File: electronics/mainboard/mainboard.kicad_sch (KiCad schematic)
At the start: 53 parts, among them J1 Conn_01x09, J10 Conn_01x08, J11 Conn_01x08, J12 Conn_01x08, J13 Conn_02x18_Odd_Even, J14 Conn_01x08, J15 Conn_01x08, J16 Conn_01x10, J17 Conn_02x03_Odd_Even, J2 Conn_01x09, J3 Conn_01x09, J4 Conn_01x09, J5 Conn_01x09, J6 Conn_01x09, J7 Conn_01x09, J8 Conn_01x09, J9 Conn_01x09

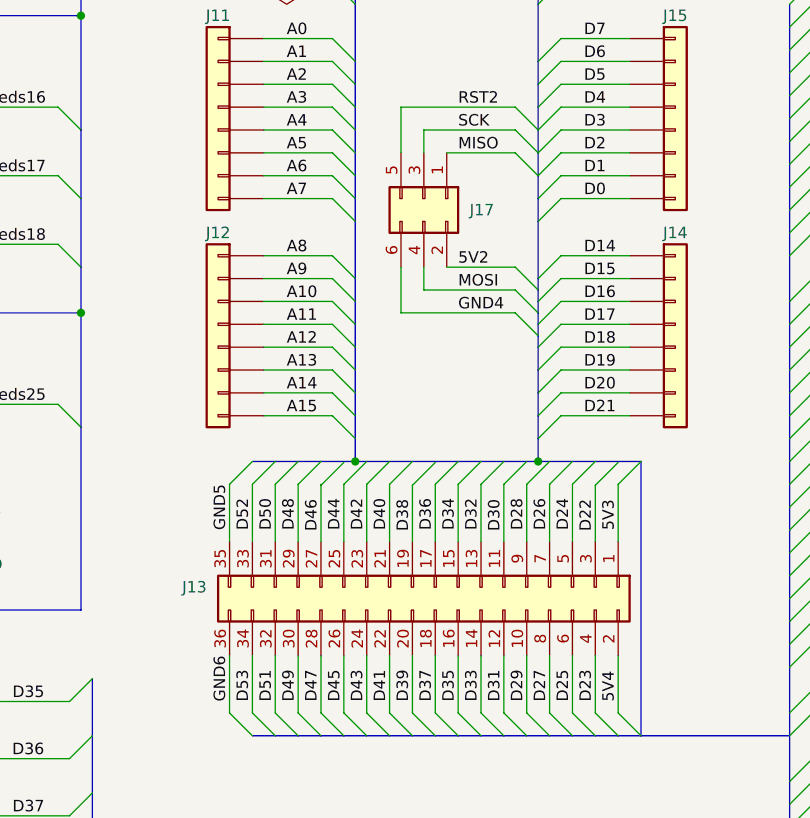
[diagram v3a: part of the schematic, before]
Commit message: place parts on pcb
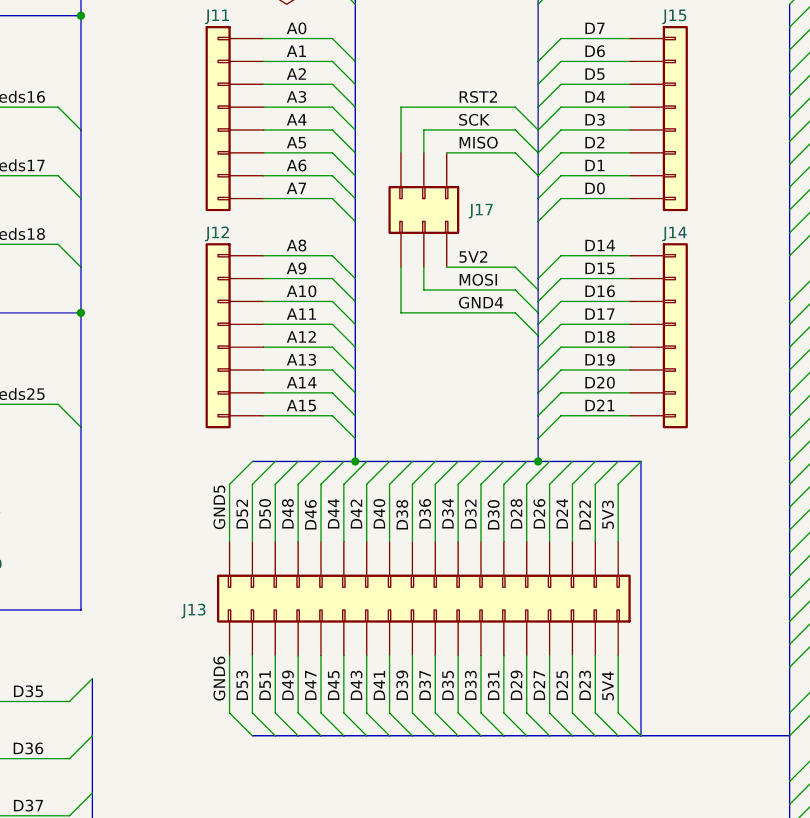
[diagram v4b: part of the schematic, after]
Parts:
- J17: footprint Connector_PinHeader_2.54mm:PinHeader_2x03_P2.54mm_Vertical_SMD -> Connector_PinSocket_2.54mm:PinSocket_2x03_P2.54mm_Vertical_SMD
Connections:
- net 5V3: now also J13.2 (Pin_2); no longer J13.1 (Pin_1)
- net 5V4: now also J13.1 (Pin_1); no longer J13.2 (Pin_2)
- net D22: now also J13.4 (Pin_4); no longer J13.3 (Pin_3)
- net D23: now also J13.3 (Pin_3); no longer J13.4 (Pin_4)
- net D24: now also J13.6 (Pin_6); no longer J13.5 (Pin_5)
- net D25: now also J13.5 (Pin_5); no longer J13.6 (Pin_6)
- net D26: now also J13.8 (Pin_8); no longer J13.7 (Pin_7)
- net D27: now also J13.7 (Pin_7); no longer J13.8 (Pin_8)
- net D28: now also J13.10 (Pin_10); no longer J13.9 (Pin_9)
- net D29: now also J13.9 (Pin_9); no longer J13.10 (Pin_10)
- net D30: now also J13.12 (Pin_12); no longer J13.11 (Pin_11)
- net D31: now also J13.11 (Pin_11); no longer J13.12 (Pin_12)
- net D32: now also J13.14 (Pin_14); no longer J13.13 (Pin_13)
- net D33: now also J13.13 (Pin_13); no longer J13.14 (Pin_14)
- net D34: now also J13.16 (Pin_16); no longer J13.15 (Pin_15)
- net D35: now also J13.15 (Pin_15); no longer J13.16 (Pin_16)
- net D36: now also J13.18 (Pin_18); no longer J13.17 (Pin_17)
- net D37: now also J13.17 (Pin_17); no longer J13.18 (Pin_18)
- net D38: now also J13.20 (Pin_20); no longer J13.19 (Pin_19)
- net D39: now also J13.19 (Pin_19); no longer J13.20 (Pin_20)
- net D40: now also J13.22 (Pin_22); no longer J13.21 (Pin_21)
- net D41: now also J13.21 (Pin_21); no longer J13.22 (Pin_22)
- net D42: now also J13.24 (Pin_24); no longer J13.23 (Pin_23)
- net D43: now also J13.23 (Pin_23); no longer J13.24 (Pin_24)
- net D44: now also J13.26 (Pin_26); no longer J13.25 (Pin_25)
- net D45: now also J13.25 (Pin_25); no longer J13.26 (Pin_26)
- net D46: now also J13.28 (Pin_28); no longer J13.27 (Pin_27)
- net D47: now also J13.27 (Pin_27); no longer J13.28 (Pin_28)
- net D48: now also J13.30 (Pin_30); no longer J13.29 (Pin_29)
- net D49: now also J13.29 (Pin_29); no longer J13.30 (Pin_30)
- net D50: now also J13.32 (Pin_32); no longer J13.31 (Pin_31)
- net D51: now also J13.31 (Pin_31); no longer J13.32 (Pin_32)
- net D52: now also J13.34 (Pin_34); no longer J13.33 (Pin_33)
- net D53: now also J13.33 (Pin_33); no longer J13.34 (Pin_34)
- net GND5: now also J13.36 (Pin_36); no longer J13.35 (Pin_35)
- net GND6: now also J13.35 (Pin_35); no longer J13.36 (Pin_36)
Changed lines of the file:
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@@
     (stroke (width 0) (type default) (color 0 0 0 0))
   )
-  (bus_entry (at 166.37 95.3582) (size 2.54 -2.54)
+  (bus_entry (at 166.37 95.25) (size 2.54 -2.54)
     (stroke (width 0) (type default) (color 0 0 0 0))
   )
@@
     (stroke (width 0) (type default) (color 0 0 0 0))
   )
-  (bus_entry (at 146.05 95.3582) (size 2.54 -2.54)
+  (bus_entry (at 146.05 95.25) (size 2.54 -2.54)
     (stroke (width 0) (type default) (color 0 0 0 0))
   )
@@
     (stroke (width 0) (type default) (color 0 0 0 0))
   )
-  (bus_entry (at 135.89 95.3582) (size 2.54 -2.54)
+  (bus_entry (at 135.89 95.25) (size 2.54 -2.54)
     (stroke (width 0) (type default) (color 0 0 0 0))
   )
@@
     (stroke (width 0) (type default) (color 0 0 0 0))
   )
-  (bus (pts (xy 151.13 92.71) (xy 146.05 92.71))
+  (bus (pts (xy 151.13 92.71) (xy 148.59 92.71))
     (stroke (width 0) (type default) (color 0 0 0 0))
   )
@@
     (stroke (width 0) (type default) (color 0 0 0 0))
   )
-  (bus (pts (xy 135.89 92.71) (xy 139.7 92.71))
+  (bus (pts (xy 135.89 92.71) (xy 138.43 92.71))
     (stroke (width 0) (type default) (color 0 0 0 0))
   )
@@
     (stroke (width 0) (type default) (color 0 0 0 0))
   )
-  (wire (pts (xy 144.78 53.34) (xy 144.78 58.42))
-    (stroke (width 0) (type default) (color 0 0 0 0))
-  )
   (wire (pts (xy 81.28 176.53) (xy 91.44 176.53))
     (stroke (width 0) (type default) (color 0 0 0 0))
@@
     (stroke (width 0) (type default) (color 0 0 0 0))
   )
-  (bus (pts (xy 166.37 92.71) (xy 171.45 92.71))
+  (bus (pts (xy 166.37 92.71) (xy 168.91 92.71))
     (stroke (width 0) (type default) (color 0 0 0 0))
   )
@@
     (stroke (width 0) (type default) (color 0 0 0 0))
   )
-  (wire (pts (xy 147.32 71.12) (xy 147.32 73.66))
-    (stroke (width 0) (type default) (color 0 0 0 0))
-  )
   (wire (pts (xy 162.56 58.42) (xy 170.18 58.42))
     (stroke (width 0) (type default) (color 0 0 0 0))
@@
     (stroke (width 0) (type default) (color 0 0 0 0))
   )
-  (wire (pts (xy 147.32 55.88) (xy 157.48 55.88))
-    (stroke (width 0) (type default) (color 0 0 0 0))
-  )
   (wire (pts (xy 148.59 114.3) (xy 148.59 120.65))
     (stroke (width 0) (type default) (color 0 0 0 0))
@@
     (stroke (width 0) (type default) (color 0 0 0 0))
   )
+  (wire (pts (xy 147.32 55.88) (xy 157.48 55.88))
+    (stroke (width 0) (type default) (color 0 0 0 0))
+  )
   (bus (pts (xy 78.74 135.89) (xy 78.74 142.24))
     (stroke (width 0) (type default) (color 0 0 0 0))
@@
     (stroke (width 0) (type default) (color 0 0 0 0))
   )
-  (wire (pts (xy 166.37 95.3582) (xy 166.37 101.6))
+  (wire (pts (xy 166.37 95.25) (xy 166.37 101.6))
     (stroke (width 0) (type default) (color 0 0 0 0))
   )
@@
     (stroke (width 0) (type default) (color 0 0 0 0))
   )
-  (wire (pts (xy 144.78 71.12) (xy 144.78 76.2))
-    (stroke (width 0) (type default) (color 0 0 0 0))
-  )
   (wire (pts (xy 63.5 119.38) (xy 72.39 119.38))
     (stroke (width 0) (type default) (color 0 0 0 0))
@@
     (stroke (width 0) (type default) (color 0 0 0 0))
   )
+  (wire (pts (xy 157.48 73.66) (xy 147.32 73.66))
+    (stroke (width 0) (type default) (color 0 0 0 0))
+  )
   (bus (pts (xy 78.74 109.22) (xy 109.22 109.22))
     (stroke (width 0) (type default) (color 0 0 0 0))
@@
     (stroke (width 0) (type default) (color 0 0 0 0))
   )
-  (wire (pts (xy 146.05 95.3582) (xy 146.05 101.6))
+  (wire (pts (xy 146.05 95.25) (xy 146.05 101.6))
     (stroke (width 0) (type default) (color 0 0 0 0))
   )
@@
     (stroke (width 0) (type default) (color 0 0 0 0))
   )
+  (wire (pts (xy 144.78 71.12) (xy 144.78 76.2))
+    (stroke (width 0) (type default) (color 0 0 0 0))
+  )
   (wire (pts (xy 128.27 95.25) (xy 128.27 101.6))
     (stroke (width 0) (type default) (color 0 0 0 0))
@@
     (stroke (width 0) (type default) (color 0 0 0 0))
   )
+  (bus (pts (xy 138.43 92.71) (xy 139.7 92.71))
+    (stroke (width 0) (type default) (color 0 0 0 0))
+  )
   (bus (pts (xy 276.86 128.27) (xy 276.86 130.81))
     (stroke (width 0) (type default) (color 0 0 0 0))
@@
     (stroke (width 0) (type default) (color 0 0 0 0))
   )
-  (wire (pts (xy 135.89 95.3582) (xy 135.89 101.6))
+  (wire (pts (xy 135.89 95.25) (xy 135.89 101.6))
     (stroke (width 0) (type default) (color 0 0 0 0))
   )
@@
     (stroke (width 0) (type default) (color 0 0 0 0))
   )
+  (wire (pts (xy 147.32 73.66) (xy 147.32 71.12))
+    (stroke (width 0) (type default) (color 0 0 0 0))
+  )
   (wire (pts (xy 190.5 62.23) (xy 199.39 62.23))
     (stroke (width 0) (type default) (color 0 0 0 0))
@@
     (stroke (width 0) (type default) (color 0 0 0 0))
   )
+  (wire (pts (xy 144.78 53.34) (xy 144.78 58.42))
+    (stroke (width 0) (type default) (color 0 0 0 0))
+  )
   (bus (pts (xy 43.18 109.22) (xy 43.18 116.84))
     (stroke (width 0) (type default) (color 0 0 0 0))
@@
     (stroke (width 0) (type default) (color 0 0 0 0))
   )
+  (bus (pts (xy 168.91 92.71) (xy 171.45 92.71))
+    (stroke (width 0) (type default) (color 0 0 0 0))
+  )
   (wire (pts (xy 231.14 27.94) (xy 231.14 20.32))
     (stroke (width 0) (type default) (color 0 0 0 0))
@@
     (stroke (width 0) (type default) (color 0 0 0 0))
   )
+  (bus (pts (xy 148.59 92.71) (xy 146.05 92.71))
+    (stroke (width 0) (type default) (color 0 0 0 0))
+  )
   (wire (pts (xy 129.54 82.55) (xy 137.16 82.55))
     (stroke (width 0) (type default) (color 0 0 0 0))
@@
     (stroke (width 0) (type default) (color 0 0 0 0))
   )
-  (wire (pts (xy 147.32 73.66) (xy 157.48 73.66))
-    (stroke (width 0) (type default) (color 0 0 0 0))
-  )
   (bus (pts (xy 43.18 154.94) (xy 43.18 161.29))
     (stroke (width 0) (type default) (color 0 0 0 0))
@@
     (stroke (width 0) (type default) (color 0 0 0 0))
   )
-  (wire (pts (xy 135.89 95.25) (xy 135.89 95.3582))
-    (stroke (width 0) (type default) (color 0 0 0 0))
-  )
   (bus (pts (xy 160.02 78.74) (xy 160.02 80.01))
     (stroke (width 0) (type default) (color 0 0 0 0))
@@
     (pin "2")
   )
-  (symbol (lib_id "Connector_Generic:Conn_02x18_Odd_Even") (at 148.59 106.68 270) (unit 1)
+  (symbol (lib_id "Connector_Generic:Conn_02x18_Odd_Even") (at 148.59 109.22 270) (mirror x) (unit 1)
     (in_bom yes) (on_board yes)
-    (property "Reference" "J13" (id 0) (at 123.19 106.68 90)
+    (property "Reference" "J13" (id 0) (at 123.19 109.22 90)
       (effects (font (size 1.27 1.27)) (justify right))
     )
-    (property "Value" "Conn_02x18_Odd_Even" (id 1) (at 123.19 109.2199 90)
+    (property "Value" "Conn_02x18_Odd_Even" (id 1) (at 123.19 106.6801 90)
       (effects (font (size 1.27 1.27)) (justify right) hide)
     )
-    (property "Footprint" "Connector_PinHeader_2.54mm:PinHeader_2x18_P2.54mm_Vertical_SMD" (id 2) (at 148.59 106.68 0)
+    (property "Footprint" "Connector_PinHeader_2.54mm:PinHeader_2x18_P2.54mm_Vertical_SMD" (id 2) (at 148.59 109.22 0)
       (effects (font (size 1.27 1.27)) hide)
     )
-    (property "Datasheet" "~" (id 3) (at 148.59 106.68 0)
+    (property "Datasheet" "~" (id 3) (at 148.59 109.22 0)
       (effects (font (size 1.27 1.27)) hide)
     )
@@
       (effects (font (size 1.27 1.27)) hide)
     )
-    (property "Footprint" "Connector_PinHeader_2.54mm:PinHeader_2x03_P2.54mm_Vertical_SMD" (id 2) (at 147.32 63.5 0)
+    (property "Footprint" "Connector_PinSocket_2.54mm:PinSocket_2x03_P2.54mm_Vertical_SMD" (id 2) (at 147.32 63.5 0)
       (effects (font (size 1.27 1.27)) hide)
     )
@@
     )
     (path "/71fe7ce2-86df-4a8c-bfd2-8ab532fe558d"
-      (reference "J17") (unit 1) (value "Conn_02x03_Odd_Even") (footprint "Connector_PinHeader_2.54mm:PinHeader_2x03_P2.54mm_Vertical_SMD")
+      (reference "J17") (unit 1) (value "Conn_02x03_Odd_Even") (footprint "Connector_PinSocket_2.54mm:PinSocket_2x03_P2.54mm_Vertical_SMD")
     )
     (path "/ba17e16f-e091-4eea-a534-e79da372956f"

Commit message: route pcb
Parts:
- removed NT10: NetTie_2, NetTie:NetTie-2_SMD_Pad0.5mm, symbol Device:NetTie_2
- NT1, NT2, NT3, NT4, NT5, NT6, NT7, NT8, NT9: footprint NetTie:NetTie-2_SMD_Pad0.5mm -> NetTie:NetTie-2_SMD_Pad2.0mm
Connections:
- net +5V: no longer NT4.1
- net 5V3: no longer NT3.2
- net 5V4: now also NT3.2; no longer NT4.2
- net D22: now also R24.2; no longer R1.2
- net D23: now also R3.2; no longer R2.2
- net D24: now also R21.2; no longer R3.2
- net D25: now also R6.2; no longer R4.2
- net D26: now also R18.2; no longer R5.2
- net D27: now also R9.2; no longer R6.2
- net D28: now also R15.2; no longer R7.2
- net D29: now also R12.2; no longer R8.2
- net D30: no longer R9.2
- net D31: no longer R10.2
- net D32: no longer R11.2
- net D33: no longer R12.2
- net D34: now also R23.2; no longer R13.2
- net D35: now also R2.2; no longer R14.2
- net D36: now also R20.2; no longer R15.2
- net D37: now also R5.2; no longer R16.2
- net D39: now also R8.2; no longer R18.2
- net D40: now also R14.2; no longer R19.2
- net D41: now also R11.2; no longer R20.2
- net D42: now also R25.2; no longer R21.2
- net D43: no longer R22.2
- net D44: now also R22.2
- net D45: now also R1.2
- net D46: now also R19.2
- net D47: now also R4.2; no longer R23.2
- net D48: now also R16.2; no longer R24.2
- net D49: now also R7.2; no longer R25.2
- net D50: now also R13.2
- net D51: now also R10.2
- net GND: now also NT4.1
- net GND1: now also NT4.2; no longer NT5.2
- net GND2: now also NT5.2; no longer NT6.2
- net GND3: now also NT6.2; no longer NT7.2
- net GND4: now also NT7.2; no longer NT8.2
- net GND5: now also NT8.2; no longer NT9.2
- net GND6: now also NT9.2
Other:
- moved on the sheet: NT4, NT5, NT6, NT7, NT8, NT9

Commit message: add project and version information
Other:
- title: (none) -> Mainboard
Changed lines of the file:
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@@
 (kicad_sch (version 20211123) (generator eeschema)
   (paper "A4")
+  (title_block
+    (title "Mainboard")
+    (comment 1 "${PROJECT}")
+    (comment 2 "${PROJECT-URL}")
+    (comment 3 "${GIT-COMMIT-HASH}")
+    (comment 4 "${GIT-COMMIT-TAG}")
+  )
   (junction (at 152.4 180.34) (diameter 0) (color 0 0 0 0)
   )

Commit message: solve erc and drc problems
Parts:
- added H1, H2: MountingHole, MountingHole:MountingHole_3.2mm_M3, symbol Mechanical:MountingHole
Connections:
- no-connect marks 3 -> 4
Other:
- moved on the sheet: NT3, NT4, NT5, NT6, NT7, NT8, NT9

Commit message: exclude some parts from bom
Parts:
- NT1, NT2, NT3, NT4, NT5, NT6, NT7, NT8, NT9, XA1: now left out of the parts list
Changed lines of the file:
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@@
   )
   (symbol (lib_id "arduino:Arduino_Mega2560_Shield") (at 232.41 93.98 0) (unit 1)
-    (in_bom yes) (on_board yes)
+    (in_bom no) (on_board yes)
     (property "Reference" "XA1" (id 0) (at 209.55 31.75 0)
       (effects (font (size 1.524 1.524)))
@@
   )
   (symbol (lib_id "Device:NetTie_2") (at 146.05 182.88 0) (unit 1)
-    (in_bom yes) (on_board yes)
+    (in_bom no) (on_board yes)
     (property "Reference" "NT6" (id 0) (at 146.05 181.61 0))
     (property "Value" "NetTie_2" (id 1) (at 146.05 180.34 0)
@@
   )
   (symbol (lib_id "Device:NetTie_2") (at 146.05 194.31 0) (unit 1)
-    (in_bom yes) (on_board yes)
+    (in_bom no) (on_board yes)
     (property "Reference" "NT9" (id 0) (at 146.05 193.04 0))
     (property "Value" "NetTie_2" (id 1) (at 146.05 191.77 0)
@@
   )
   (symbol (lib_id "Device:NetTie_2") (at 146.05 179.07 0) (unit 1)
-    (in_bom yes) (on_board yes)
+    (in_bom no) (on_board yes)
     (property "Reference" "NT5" (id 0) (at 146.05 177.8 0))
     (property "Value" "NetTie_2" (id 1) (at 146.05 176.53 0)
@@
   )
   (symbol (lib_id "Device:NetTie_2") (at 146.05 175.26 0) (unit 1)
-    (in_bom yes) (on_board yes)
+    (in_bom no) (on_board yes)
     (property "Reference" "NT4" (id 0) (at 146.05 173.99 0))
     (property "Value" "NetTie_2" (id 1) (at 146.05 172.72 0)
@@
   )
   (symbol (lib_id "Device:NetTie_2") (at 146.05 186.69 0) (unit 1)
-    (in_bom yes) (on_board yes)
+    (in_bom no) (on_board yes)
     (property "Reference" "NT7" (id 0) (at 146.05 185.42 0))
     (property "Value" "NetTie_2" (id 1) (at 146.05 184.15 0)
@@
   )
   (symbol (lib_id "Device:NetTie_2") (at 146.05 170.18 0) (unit 1)
-    (in_bom yes) (on_board yes)
+    (in_bom no) (on_board yes)
     (property "Reference" "NT3" (id 0) (at 146.05 168.91 0))
     (property "Value" "NetTie_2" (id 1) (at 146.05 167.64 0)
@@
   )
   (symbol (lib_id "Device:NetTie_2") (at 146.05 162.56 0) (unit 1)
-    (in_bom yes) (on_board yes)
+    (in_bom no) (on_board yes)
     (property "Reference" "NT2" (id 0) (at 146.05 161.29 0))
     (property "Value" "NetTie_2" (id 1) (at 146.05 160.02 0)
@@
   )
   (symbol (lib_id "Device:NetTie_2") (at 146.05 158.75 0) (unit 1)
-    (in_bom yes) (on_board yes)
+    (in_bom no) (on_board yes)
     (property "Reference" "NT1" (id 0) (at 146.05 157.48 0))
     (property "Value" "NetTie_2" (id 1) (at 146.05 156.21 0)
@@
   )
   (symbol (lib_id "Device:NetTie_2") (at 146.05 190.5 0) (unit 1)
-    (in_bom yes) (on_board yes)
+    (in_bom no) (on_board yes)
     (property "Reference" "NT8" (id 0) (at 146.05 189.23 0))
     (property "Value" "NetTie_2" (id 1) (at 146.05 187.96 0)
